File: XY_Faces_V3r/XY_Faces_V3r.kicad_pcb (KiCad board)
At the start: 4 copper layers, 83 x 98 mm, 34 parts, among them CN1 DF11-2DSA-4DP, J2 Conn_01x01, J3 Conn_01x01, J4 Conn_01x01, J5 Conn_01x01, U1 VEML7700, U2 TMP112xxDRL, U3 DRV2605LDGS, U4 TCA4311ADGKR, U5 5040500691, U6 5040500691

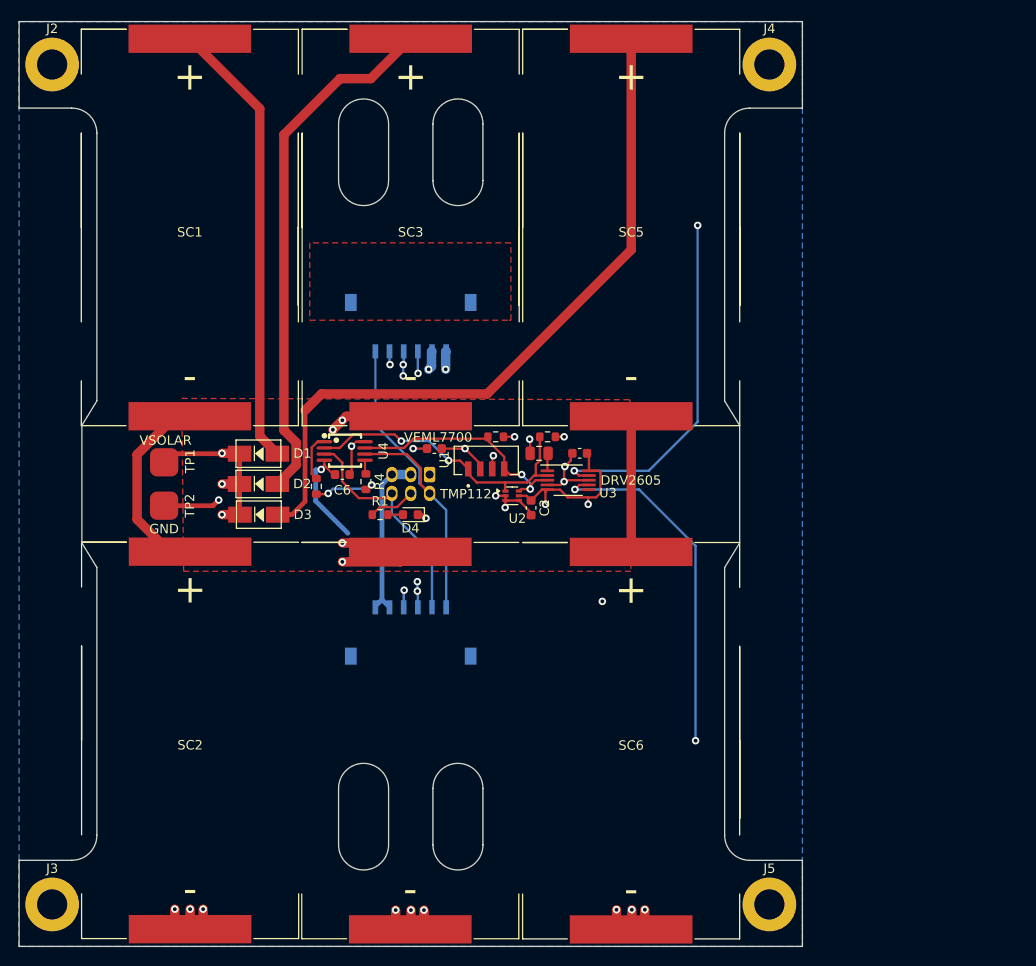
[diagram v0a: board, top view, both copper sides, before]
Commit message: Changed all Passives to 0402
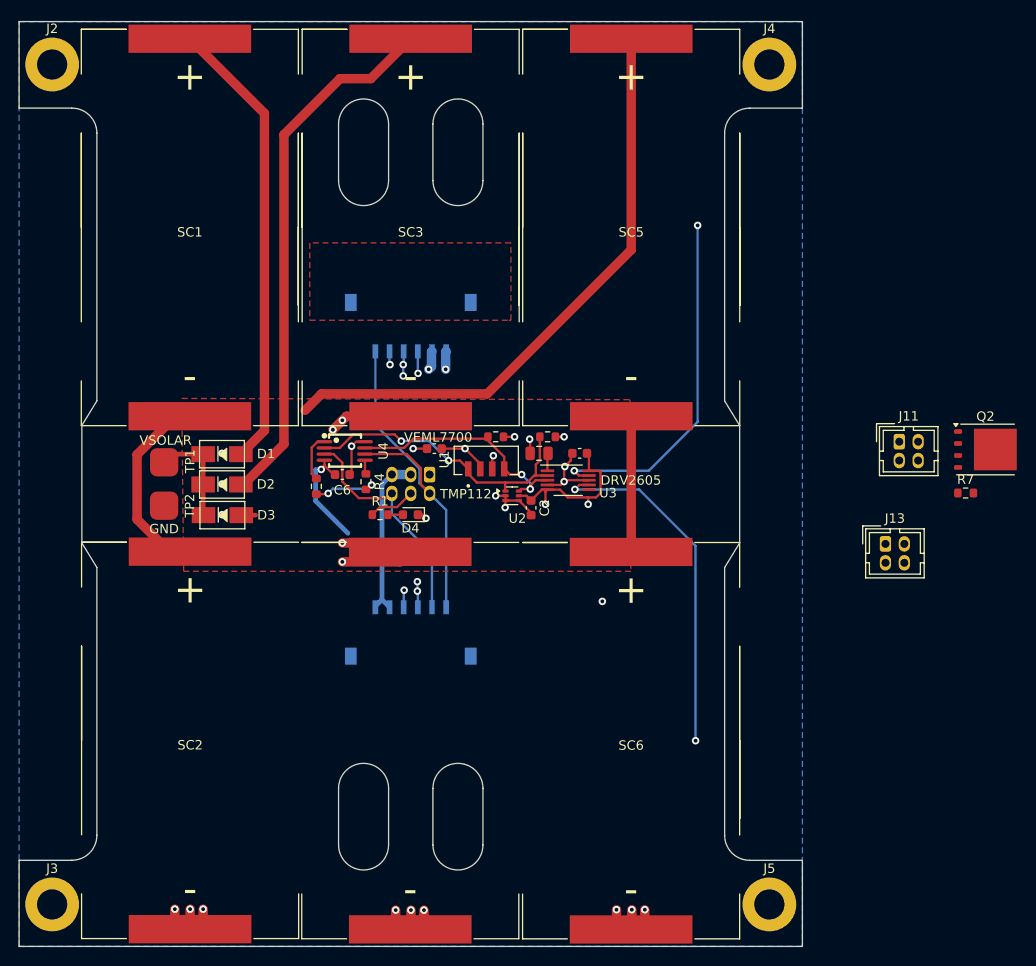
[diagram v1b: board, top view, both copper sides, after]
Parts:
- added J11: DF11-4DP-2DSA, Connector_Hirose:Hirose_DF11-4DP-2DSA_2x02_P2.00mm_Vertical, F.Cu at (196.3, 110.3)
- added J13: DF11-4DP-2DSA, Connector_Hirose:Hirose_DF11-4DP-2DSA_2x02_P2.00mm_Vertical, F.Cu at (194.8, 121.1)
- added Q2: CSD17576Q5B, Package_TO_SOT_SMD:TDSON-8-1, F.Cu at (205.4, 111.1)
- added R7: 1M, Resistor_SMD:R_0603_1608Metric, F.Cu at (203.3, 115.7)
- moved D1 3.86 mm to (124.5, 111.6)
- moved D2 3.86 mm to (124.5, 114.8)
- moved D3 3.86 mm to (124.5, 118.0)
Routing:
- net Net-(D3-A): track 77.1 -> 65.5 mm
- net VSOLAR: track 88.8 -> 80.7 mm
- net GND: track 52.5 -> 46.4 mm, vias 21 -> 20
- net Net-(D2-A): track 56.0 -> 56.8 mm
- net Net-(D1-A): track 47.8 -> 48.3 mm

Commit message: Moved Temp and Light Sensors
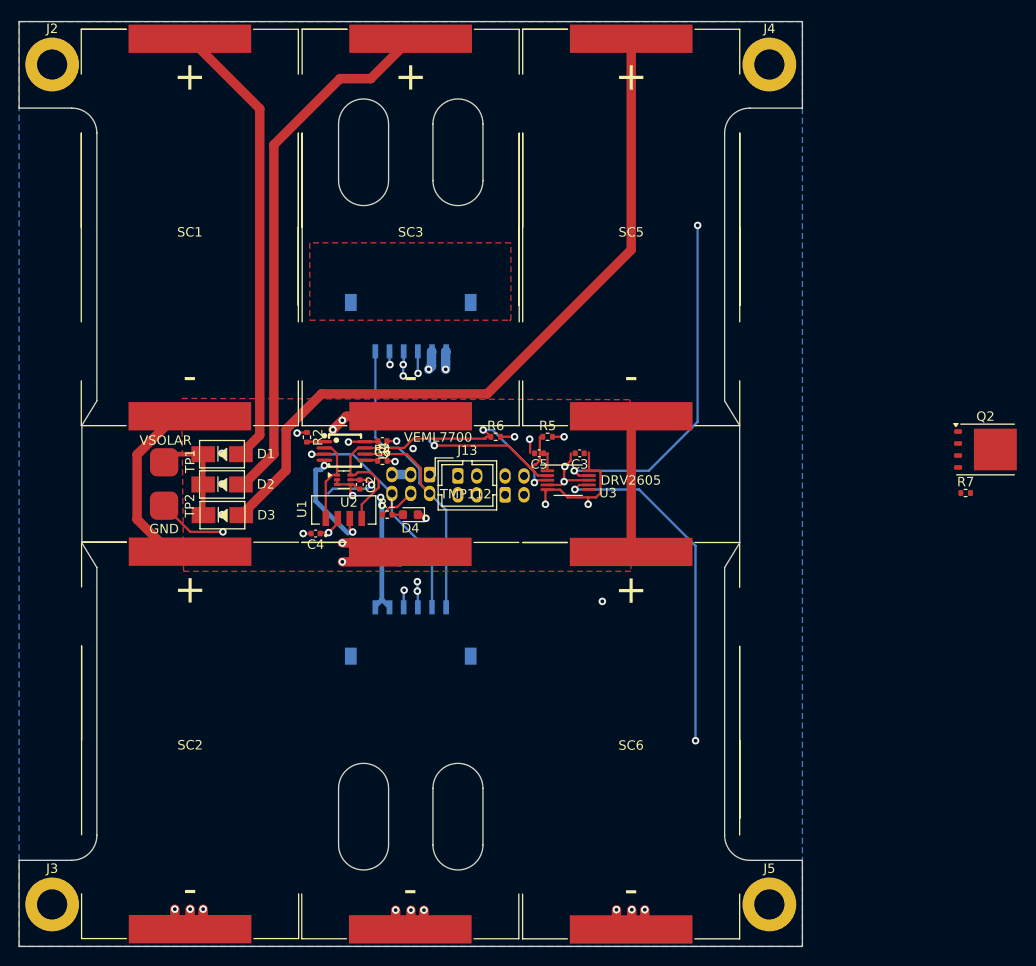
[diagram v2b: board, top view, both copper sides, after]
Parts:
- C2, C3, C4, C6: footprint Capacitor_SMD:C_0603_1608Metric -> Capacitor_SMD:C_0402_1005Metric
- C5: footprint Capacitor_SMD:C_0805_2012Metric -> Capacitor_SMD:C_0402_1005Metric
- J11: moved to B.Cu
- R1, R2, R4, R5, R6, R7: footprint Resistor_SMD:R_0603_1608Metric -> Resistor_SMD:R_0402_1005Metric
- moved J13 45.9 mm to (149.5, 113.9)
- moved J11 42.1 mm to (154.5, 115.9)
- moved C2 18.3 mm to (139.1, 114.8)
- moved U2 17.9 mm to (137.4, 114.3)
- moved U1 16.0 mm to (137.4, 117.5)
- moved C4 15.5 mm to (134.4, 120.0)
- moved C6 5.54 mm to (141.5, 110.2), turned to 180 degrees
- moved R2 5.30 mm to (133.5, 109.8), turned to -90 degrees
- moved R4 2.81 mm to (141.5, 112.3), turned to 0 degrees
- moved R1 0.75 mm to (142.0, 118.0)
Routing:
- net Net-(D3-A): track 65.5 -> 77.9 mm
- net /SDA: track 25.0 -> 37.2 mm
- net GND: track 46.4 -> 51.7 mm, vias 20 -> 22
- net +3V3: track 111.8 -> 106.6 mm, vias 12 -> 13
- net /SCL: track 32.3 -> 27.1 mm, vias 2 -> 1
- net Net-(U4-EN): track 5.09 -> 1.90 mm
- net SCLIN: track 45.7 -> 46.8 mm, vias 1 -> 2
- net VSOLAR: track 80.7 -> 81.6 mm, vias 5 -> 7
- net SDAIN: track 39.8 -> 40.6 mm

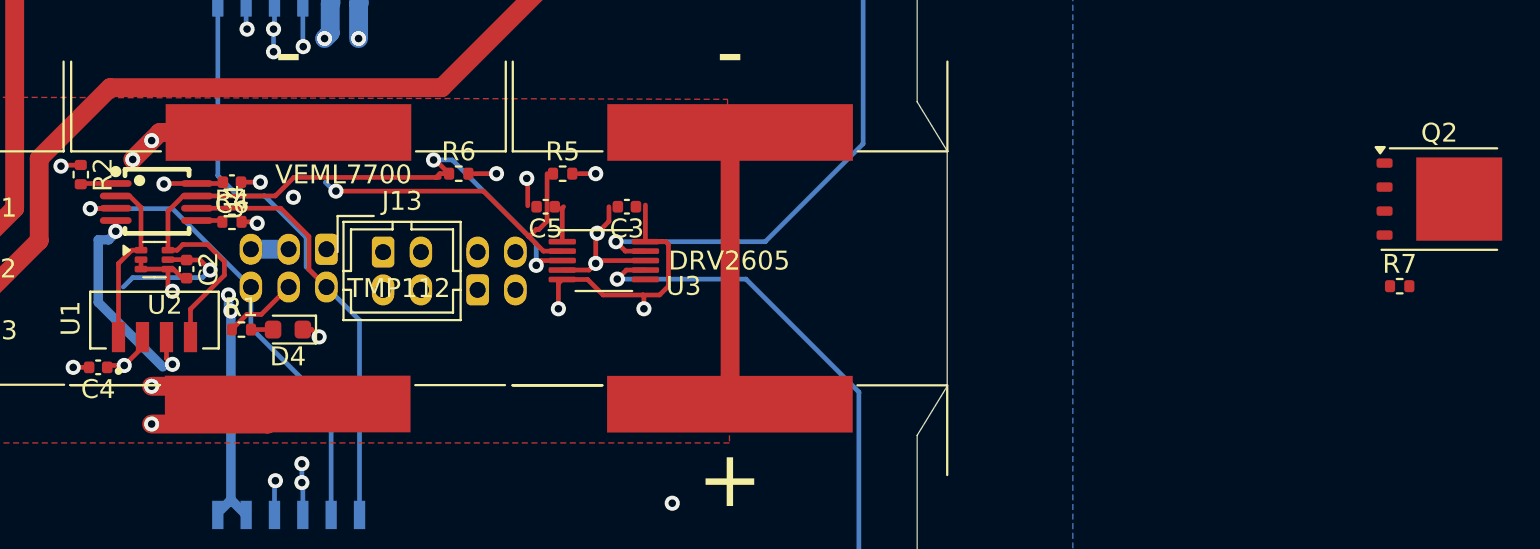
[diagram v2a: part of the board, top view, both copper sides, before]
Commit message: Wired Up RBF Port
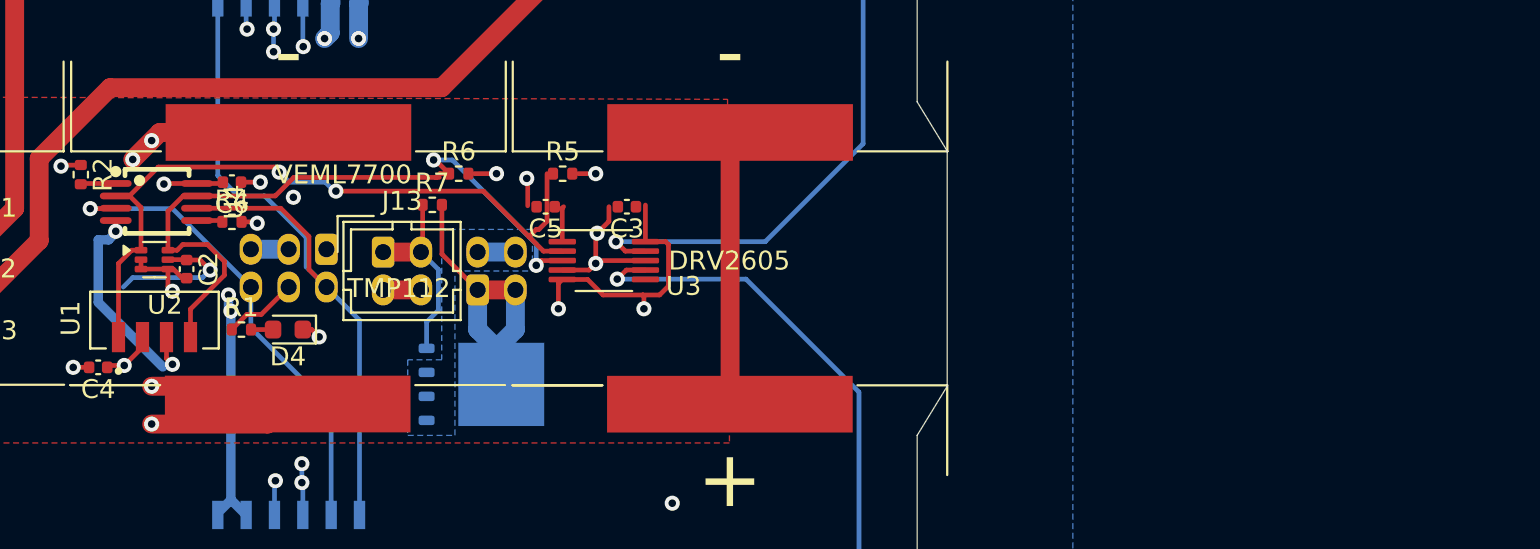
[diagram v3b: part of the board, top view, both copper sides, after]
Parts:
- Q2: moved to B.Cu
- moved Q2 51.6 mm to (154.7, 120.9)
- moved R7 51.4 mm to (152.1, 111.4)
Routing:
- net /RBF_High: track 0.00 -> 18.1 mm
- net /SCL: track 27.1 -> 39.2 mm, vias 1 -> 2
- net Net-(J13-Pin_1): track 0.00 -> 10.3 mm
- net GND: track 51.7 -> 53.7 mm
- net /RBF_Low: track 0.00 -> 2.00 mm
- added copper zone on B.Cu, net /RBF_Low

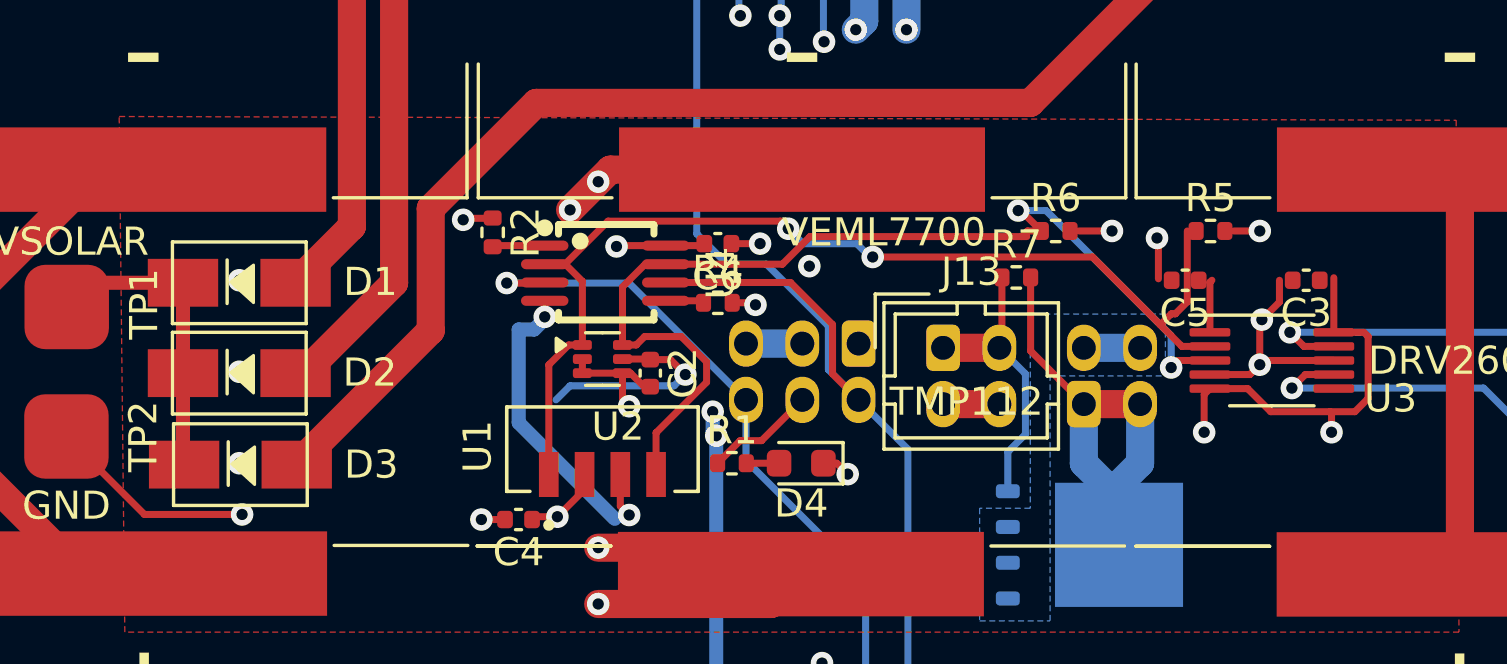
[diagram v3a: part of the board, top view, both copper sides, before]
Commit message: V3r: Cleaned Up DRC Errors
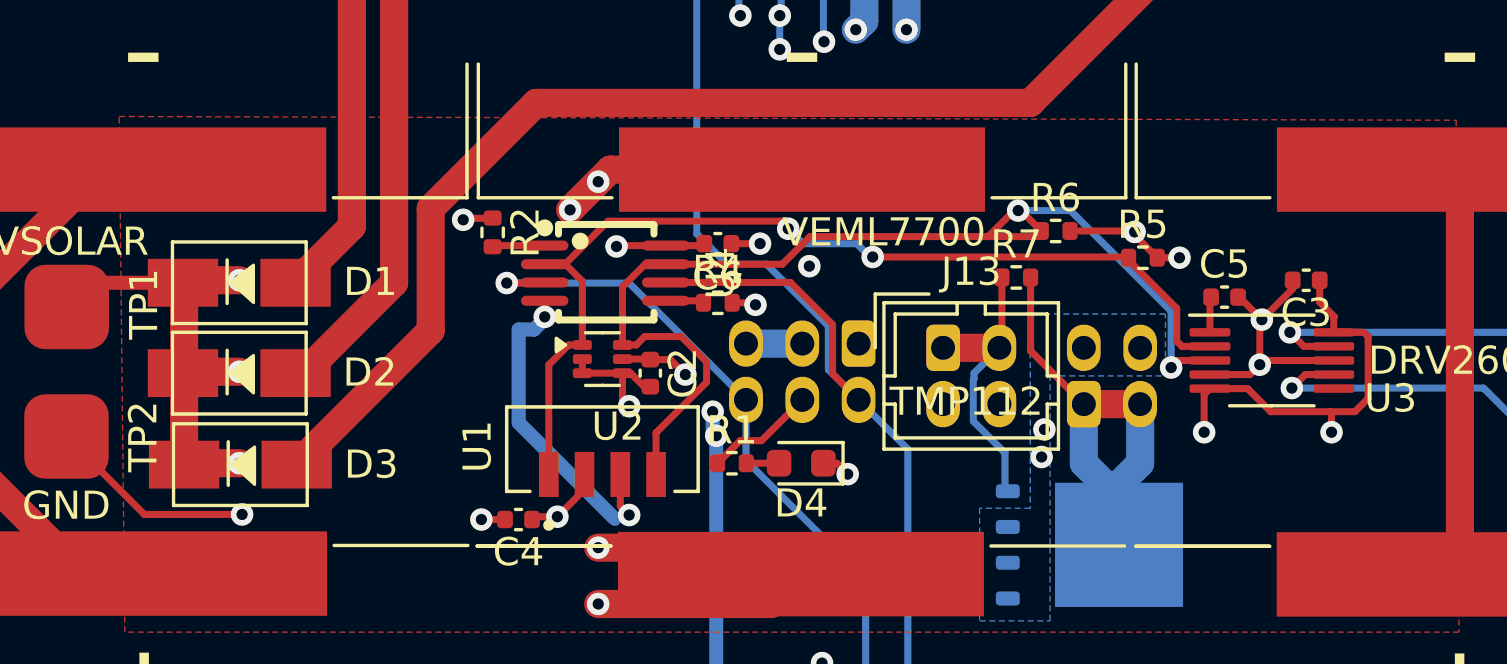
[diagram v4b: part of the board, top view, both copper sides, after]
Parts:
- moved R5 2.58 mm to (156.6, 110.7)
- moved C5 1.52 mm to (159.5, 112.1), turned to 0 degrees
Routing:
- net VSOLAR: track 81.6 -> 87.5 mm
- net /RBF_Low: track 2.00 -> 6.66 mm, vias 0 -> 2
- net /SCL: track 39.2 -> 36.0 mm
- net /SDA: track 37.2 -> 39.0 mm
- net +3V3: track 106.6 -> 105.5 mm
- net Net-(U3-REG): track 1.88 -> 1.17 mm
- net GND: track 53.7 -> 53.5 mm, vias 22 -> 21
